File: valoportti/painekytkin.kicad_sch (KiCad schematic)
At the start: 20 parts, among them Q1 BC547, Q2 BC547, Q3 BC547, Q4 BC547, Q5 BC547

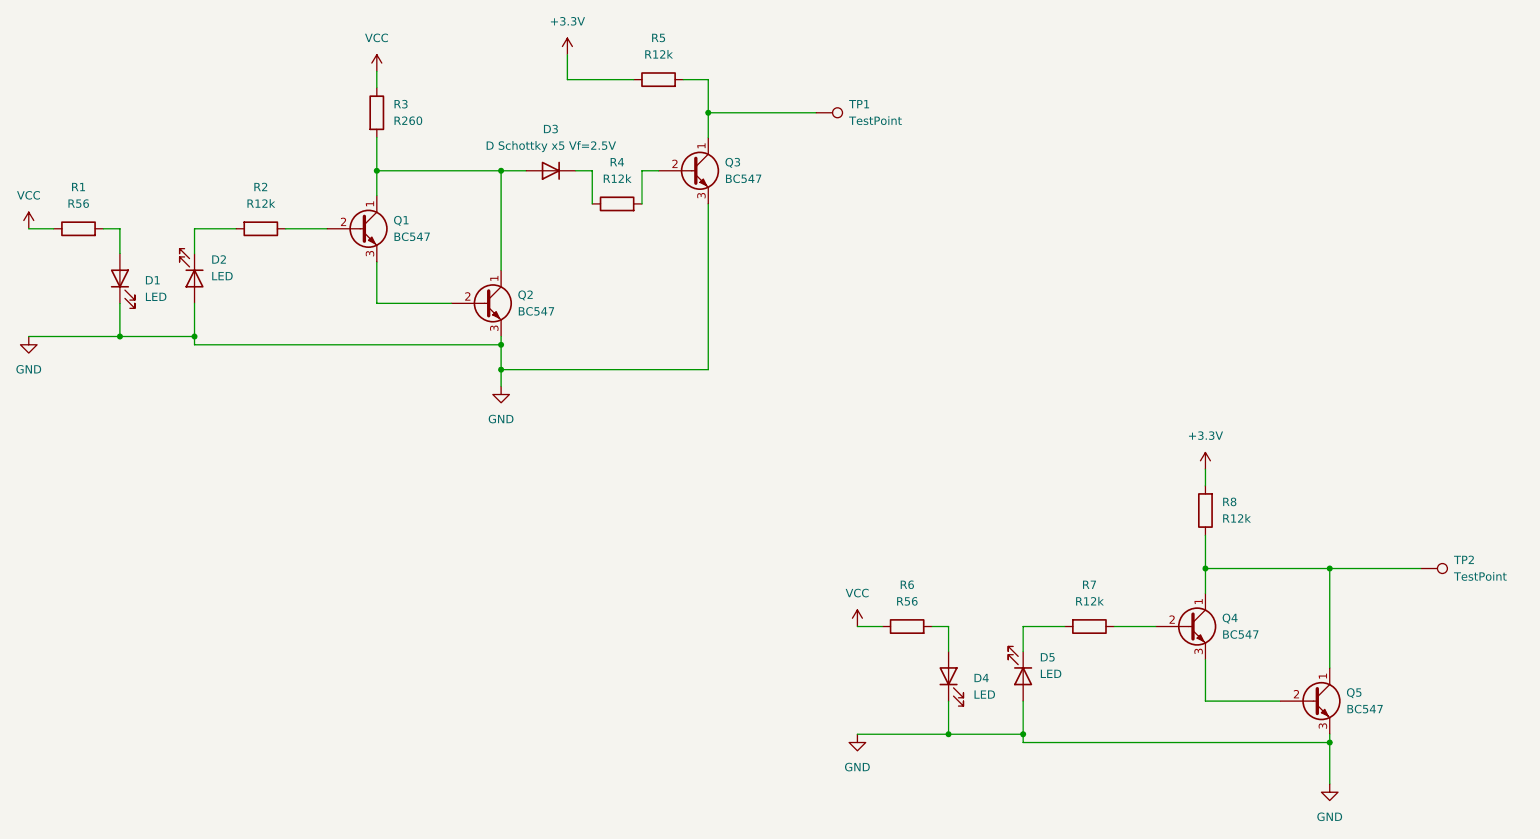
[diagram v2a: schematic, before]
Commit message: move grove lcd lib to submodule
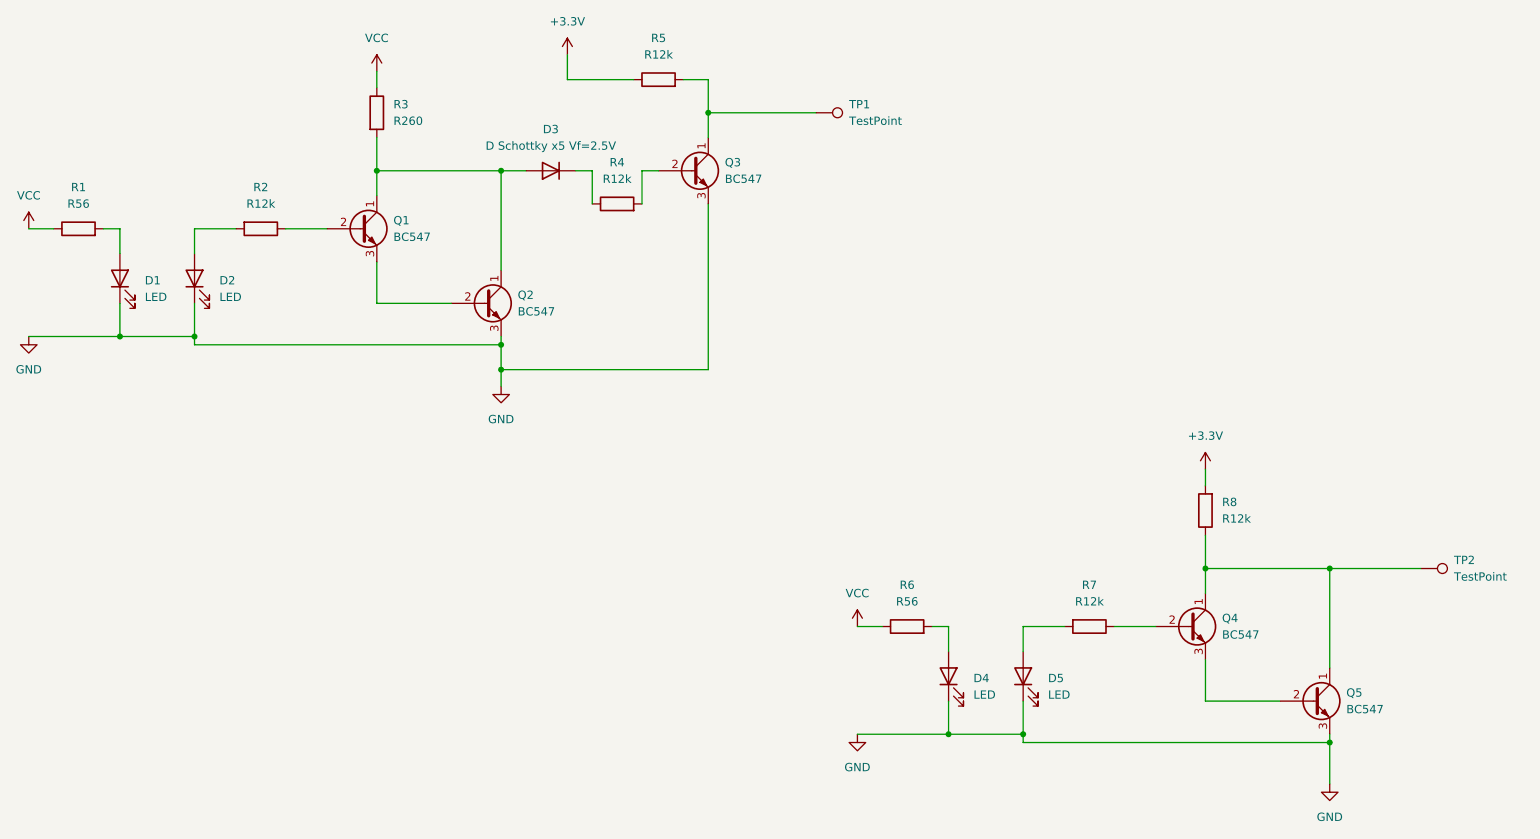
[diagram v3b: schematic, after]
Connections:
- net GND: now also D2.1 (K), D5.1 (K); no longer D2.2 (A), D5.2 (A)
- net at R7.2: now also D5.2 (A); no longer D5.1 (K)
- net at R2.2: now also D2.2 (A); no longer D2.1 (K)
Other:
- moved on the sheet: D2, D5
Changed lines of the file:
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@@
     (pin "3")
   )
-  (symbol (lib_id "Device:LED") (at 186.69 123.19 270) (unit 1)
+  (symbol (lib_id "Device:LED") (at 186.69 123.19 90) (unit 1)
     (in_bom yes) (on_board yes) (fields_autoplaced)
-    (property "Reference" "D5" (id 0) (at 189.23 120.3324 90)
-      (effects (font (size 1.27 1.27)) (justify left))
+    (property "Reference" "D5" (id 0) (at 190.5 123.5074 90)
+      (effects (font (size 1.27 1.27)) (justify right))
     )
-    (property "Value" "LED" (id 1) (at 189.23 122.8724 90)
-      (effects (font (size 1.27 1.27)) (justify left))
+    (property "Value" "LED" (id 1) (at 190.5 126.0474 90)
+      (effects (font (size 1.27 1.27)) (justify right))
     )
     (property "Footprint" "" (id 2) (at 186.69 123.19 0)
@@
     (pin "2")
   )
-  (symbol (lib_id "Device:LED") (at 59.69 62.23 270) (unit 1)
+  (symbol (lib_id "Device:LED") (at 59.69 62.23 90) (unit 1)
     (in_bom yes) (on_board yes) (fields_autoplaced)
-    (property "Reference" "D2" (id 0) (at 62.23 59.3724 90)
-      (effects (font (size 1.27 1.27)) (justify left))
+    (property "Reference" "D2" (id 0) (at 63.5 62.5474 90)
+      (effects (font (size 1.27 1.27)) (justify right))
     )
-    (property "Value" "LED" (id 1) (at 62.23 61.9124 90)
-      (effects (font (size 1.27 1.27)) (justify left))
+    (property "Value" "LED" (id 1) (at 63.5 65.0874 90)
+      (effects (font (size 1.27 1.27)) (justify right))
     )
     (property "Footprint" "" (id 2) (at 59.69 62.23 0)
